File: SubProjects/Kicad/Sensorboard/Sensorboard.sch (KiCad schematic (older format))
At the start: 12 parts, among them P1 ToyRaceCar_V2_REV3_J4, P2 ToyRaceCar_V2_REV3_J3, P3 ToyRaceCar_V2_REV3_J2, P4 ToyRaceCar_V2_REV3_J1, P5 MPU-6050, P6 ToyRaceCar_V2_REV3_J5, Q1 BSS138, Q2 BSS138

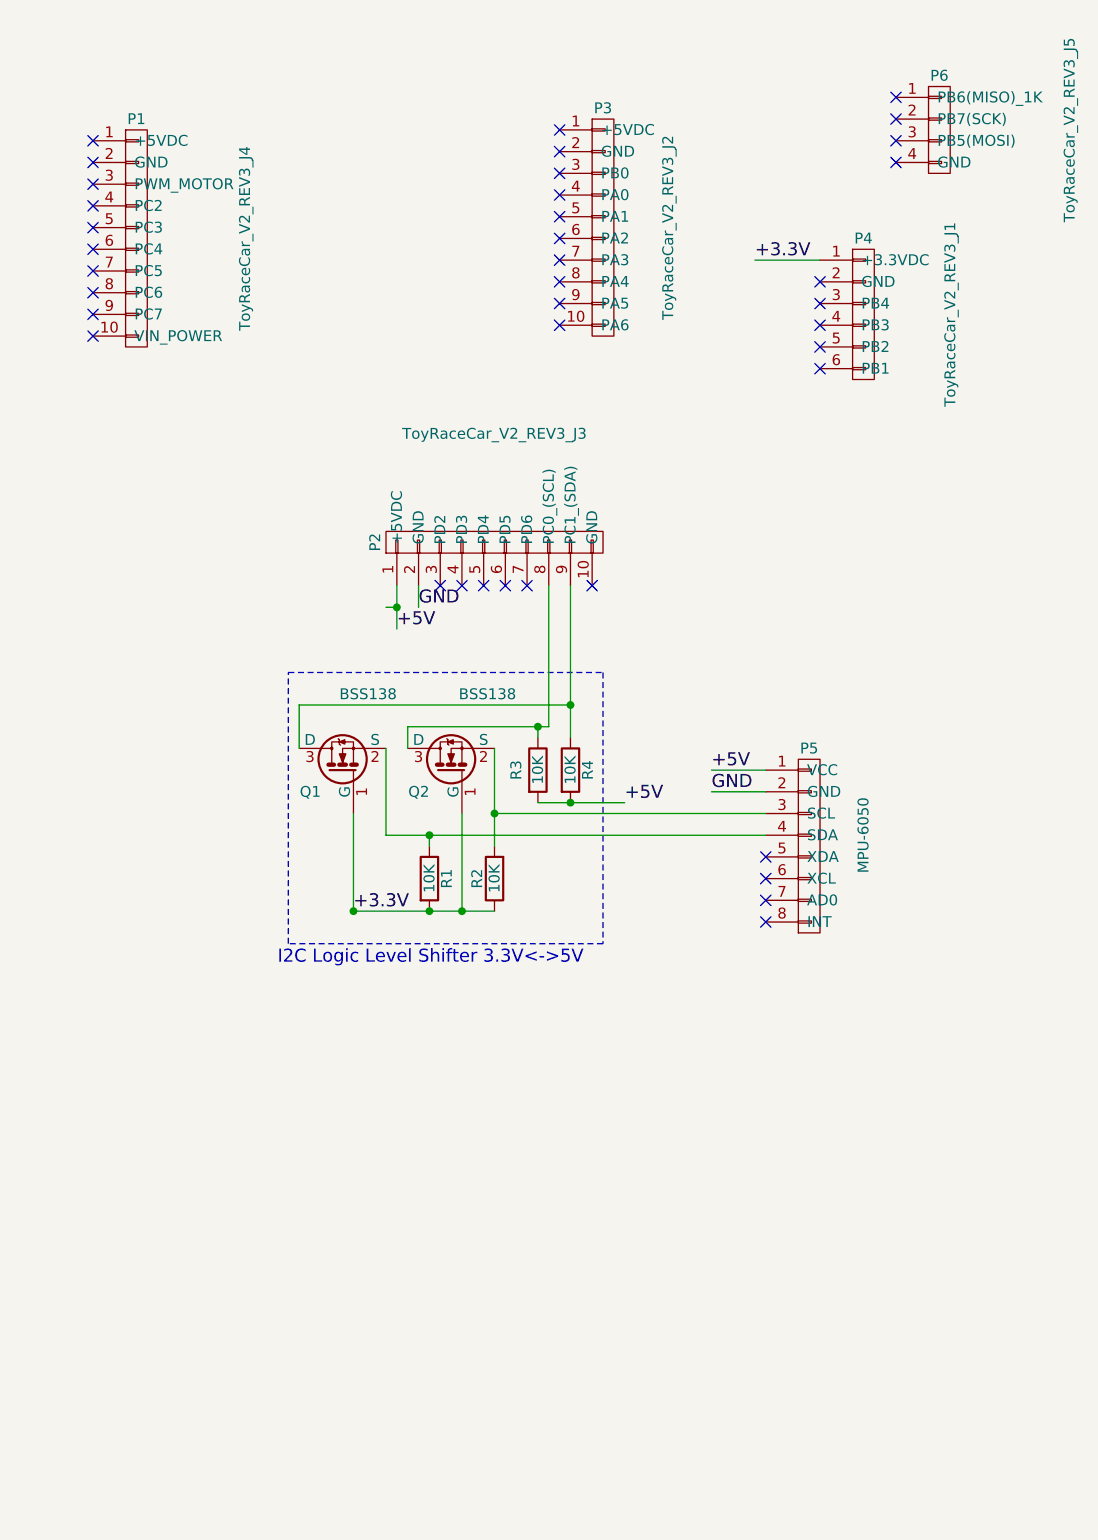
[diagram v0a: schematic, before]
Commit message: Board is designed with MPU6050, Logic Level Shifter and lap counter circuitry. Done for now.
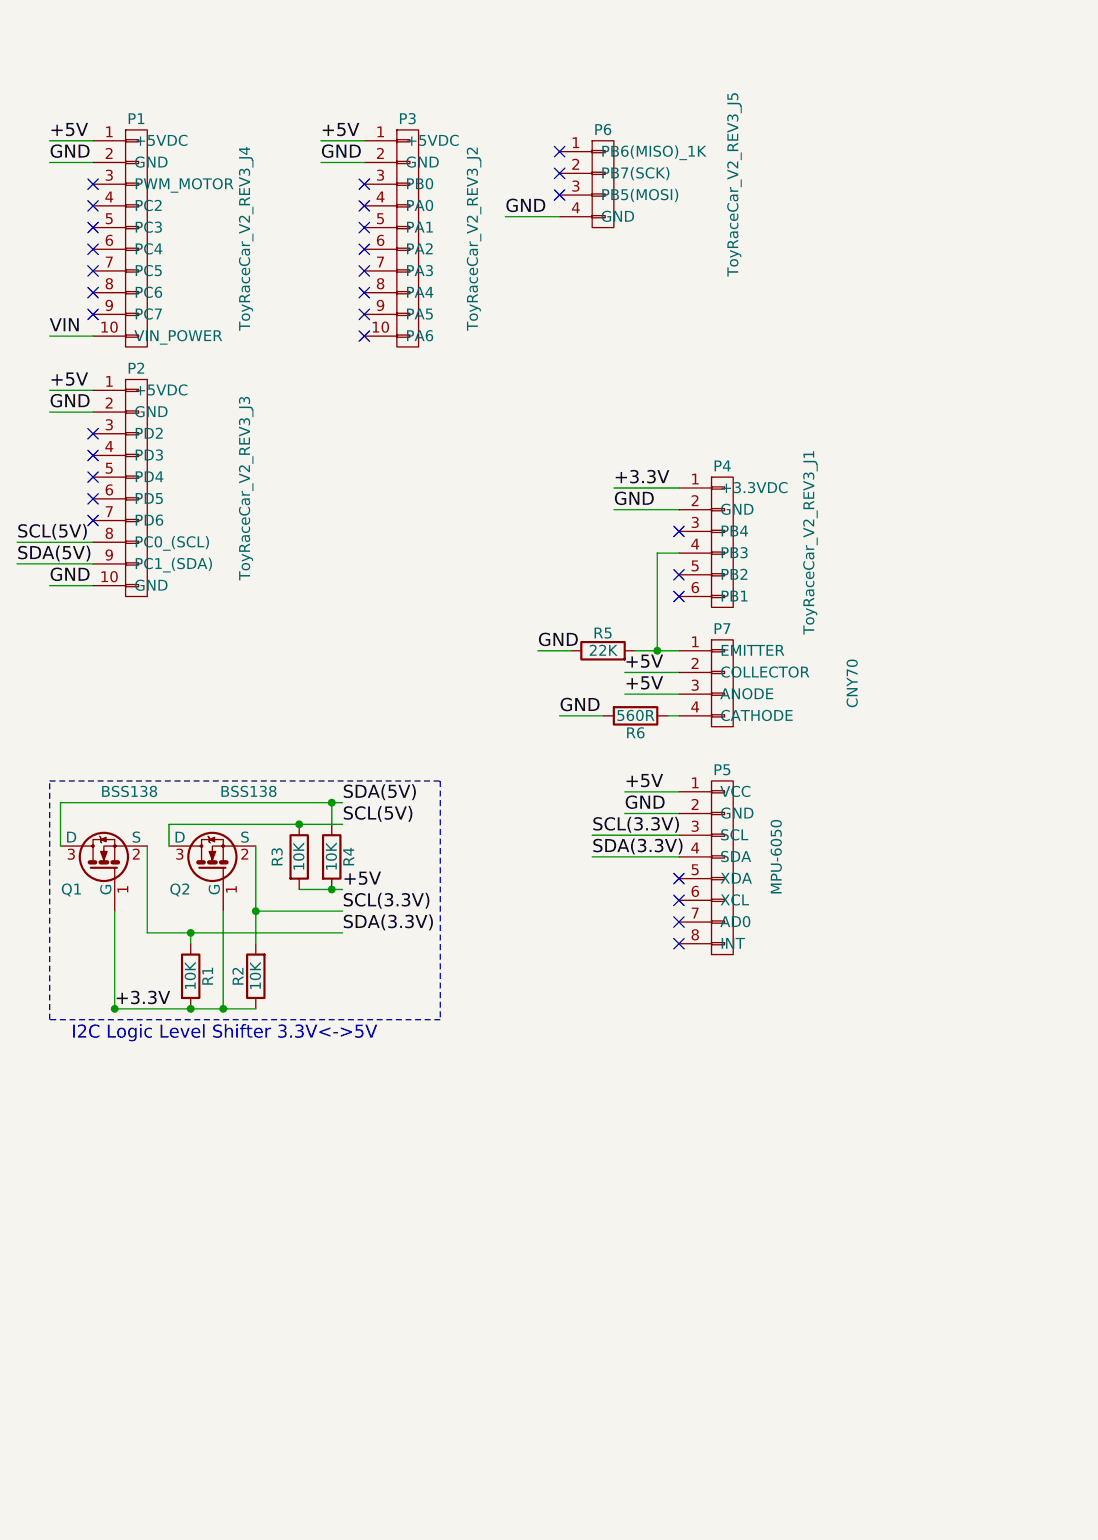
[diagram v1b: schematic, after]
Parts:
- added P7: CNY70, Sensorboard:KK254, symbol CNY70
- added R5: 22K, Resistors_SMD:R_0603_HandSoldering, symbol R
- added R6: 560R, Resistors_SMD:R_0603_HandSoldering, symbol R
- P1, P2, P3: footprint Socket_Strips:Socket_Strip_Straight_1x10 -> Pin_Headers:Pin_Header_Straight_1x10
- P4: footprint Socket_Strips:Socket_Strip_Straight_1x06 -> Pin_Headers:Pin_Header_Straight_1x06
- P5: footprint (none) -> Sensorboard:MPU-6050
- P6: footprint Socket_Strips:Socket_Strip_Straight_1x04 -> Pin_Headers:Pin_Header_Straight_1x04
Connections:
- net labels added: SCL(3.3V), SCL(5V), SDA(3.3V), SDA(5V), VIN
- wire segments 22 -> 40
- no-connect marks 39 -> 30
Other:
- moved on the sheet: P2, P3, P4, P5, P6, Q1, Q2, R1, R2, R3, R4

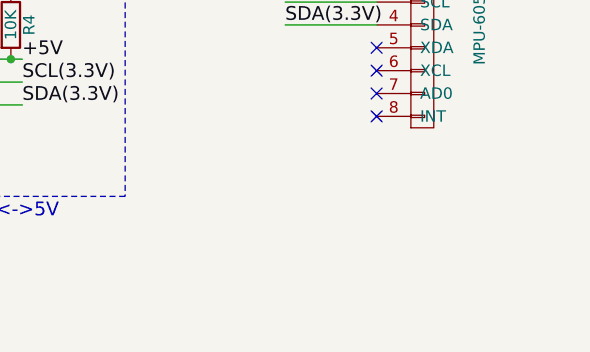
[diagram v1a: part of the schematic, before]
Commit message: Added another connector for the hall sensor
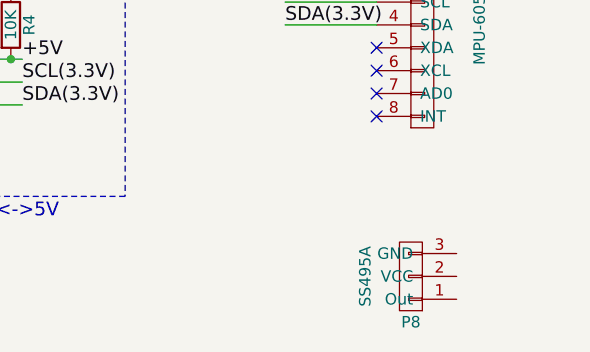
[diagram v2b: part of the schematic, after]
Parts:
- added P8: SS495A, Sensorboard:KK254-3, symbol SS495A
- P7: footprint Sensorboard:KK254 -> Sensorboard:KK254-4
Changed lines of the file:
@@
 F 0 "P7" H 3800 3650 50  0000 C CNN
 F 1 "CNY70" V 4400 3400 50  0000 C CNN
-F 2 "Sensorboard:KK254" H 3800 3400 60  0001 C CNN
+F 2 "Sensorboard:KK254-4" H 3800 3400 60  0001 C CNN
 F 3 "" H 3800 3400 60  0000 C CNN
 	1    3800 3400
@@
 Text Label 2950 3250 0    60   ~ 0
 GND
+$Comp
+L SS495A P8
+U 1 1 553E0EE3
+P 3750 5300
+F 0 "P8" H 3750 5500 50  0000 C CNN
+F 1 "SS495A" V 3950 5300 50  0000 C CNN
+F 2 "Sensorboard:KK254-3" H 3750 5300 60  0001 C CNN
+F 3 "" H 3750 5300 60  0000 C CNN
+	1    3750 5300
+	-1   0    0    1
+$EndComp
 $EndSCHEMATC

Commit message: Nearly final design. Just missing the mounting holes
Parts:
- added R10: 3K3, Resistors_SMD:R_0805_HandSoldering, symbol R
- added R11: 10K, Resistors_SMD:R_0805_HandSoldering, symbol R
- added R7, R9: 6K8, Resistors_SMD:R_0805_HandSoldering, symbol R
- added R8: 20K, Resistors_SMD:R_0805_HandSoldering, symbol R
- added RV1: 10K, Potentiometers:Potentiometer_Bourns_3006P_Angular_ScrewFront, symbol POT
- added U1: AD623AN, Housings_DIP:DIP-8__300, symbol AD623AN
- added U2: LM311N, Housings_DIP:DIP-8__300, symbol LM311N
- P8: footprint Sensorboard:KK254-3 -> (none)
- R1, R2, R3, R4: footprint Resistors_SMD:R_0603_HandSoldering -> Resistors_SMD:R_0805_HandSoldering
- R5: value 22K -> 20K; footprint Resistors_SMD:R_0603_HandSoldering -> Resistors_SMD:R_0805_HandSoldering
- R6: value 560R -> 150R; footprint Resistors_SMD:R_0603_HandSoldering -> Resistors_SMD:R_0805_HandSoldering
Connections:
- net +5V: now also P8.2 (VCC), R11.1, R9.2, RV1.1, U1.7 (V+), U2.8 (V+)
- net GND: now also P8.3 (GND), R7.2, RV1.3, U1.4 (V_), U2.1 (GND), U2.4 (V-)
- net PD6: now reaches P2.7 (PD6)
- net PD6: now also R11.2, R8.1, U2.7
- net at P8.1 (Out): now also U1.3 (+)
- new net: R10.2, U1.1 (Rg)
- new net: RV1.2, U1.2 (-)
- new net: R10.1, U1.8 (Rg)
- new net: R7.1, R8.2, R9.1, U2.2 (+)
- new net AD623AN_Out: U1.6 (OUT), U2.3 (-)
- no-connect marks 30 -> 32
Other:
- note added: "Hall Sensor Input Stage"
- moved on the sheet: P1, P2, P3, P6, Q1, Q2, R1, R2, R3, R4

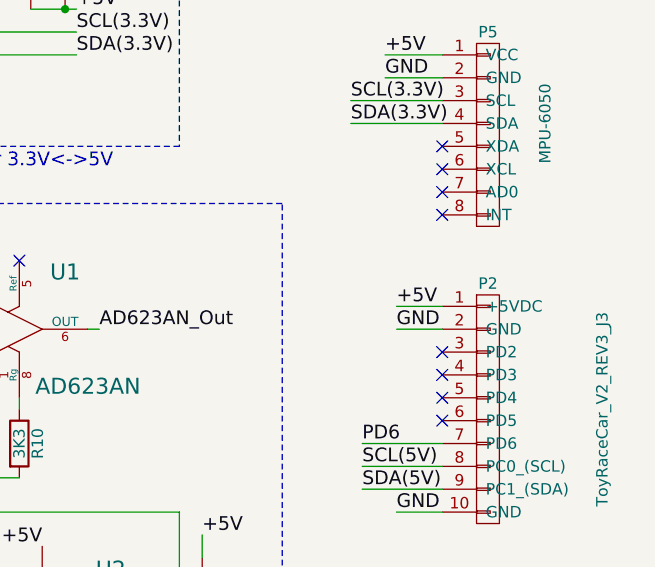
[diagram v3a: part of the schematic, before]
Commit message: Added a connection from the int pin on the mpu6050 to the int0 on the microcontroller. If we need it at some point.
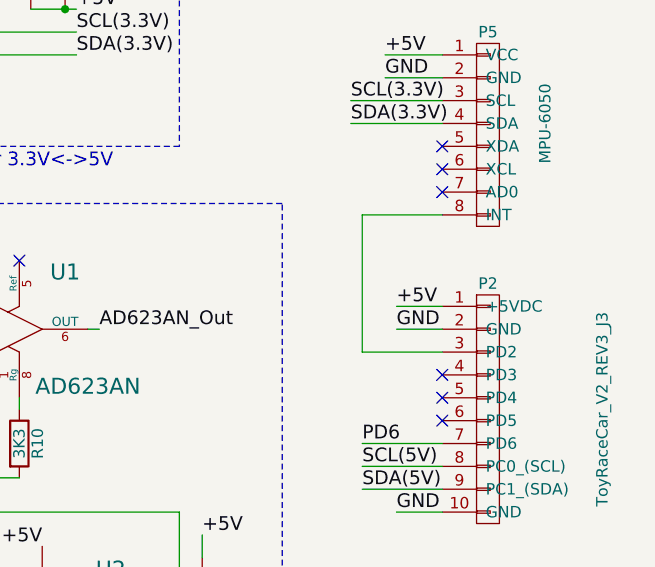
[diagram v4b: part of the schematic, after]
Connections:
- net at P2.3 (PD2): now also P5.8 (INT)
- no-connect marks 32 -> 30
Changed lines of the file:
@@
 NoConn ~ 3600 5400
 NoConn ~ 3600 5300
-NoConn ~ 3600 5200
 NoConn ~ 3600 4300
 NoConn ~ 3600 4400
 NoConn ~ 3600 4500
-NoConn ~ 3600 4600
 Text Label 3300 2500 0    60   ~ 0
 +3.3V
@@
 Text Label 750  4650 3    60   ~ 0
 GND
+Wire Wire Line
+	3600 4600 3250 4600
+Wire Wire Line
+	3250 4600 3250 5200
+Wire Wire Line
+	3250 5200 3600 5200
 $EndSCHEMATC
